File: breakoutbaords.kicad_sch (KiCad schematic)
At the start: 12 parts, among them J13 USB_A, J15 Conn_01x16, J16 Conn_01x16, J3 Conn_01x12, J4 Conn_01x12, U3 AMS1117-3.3

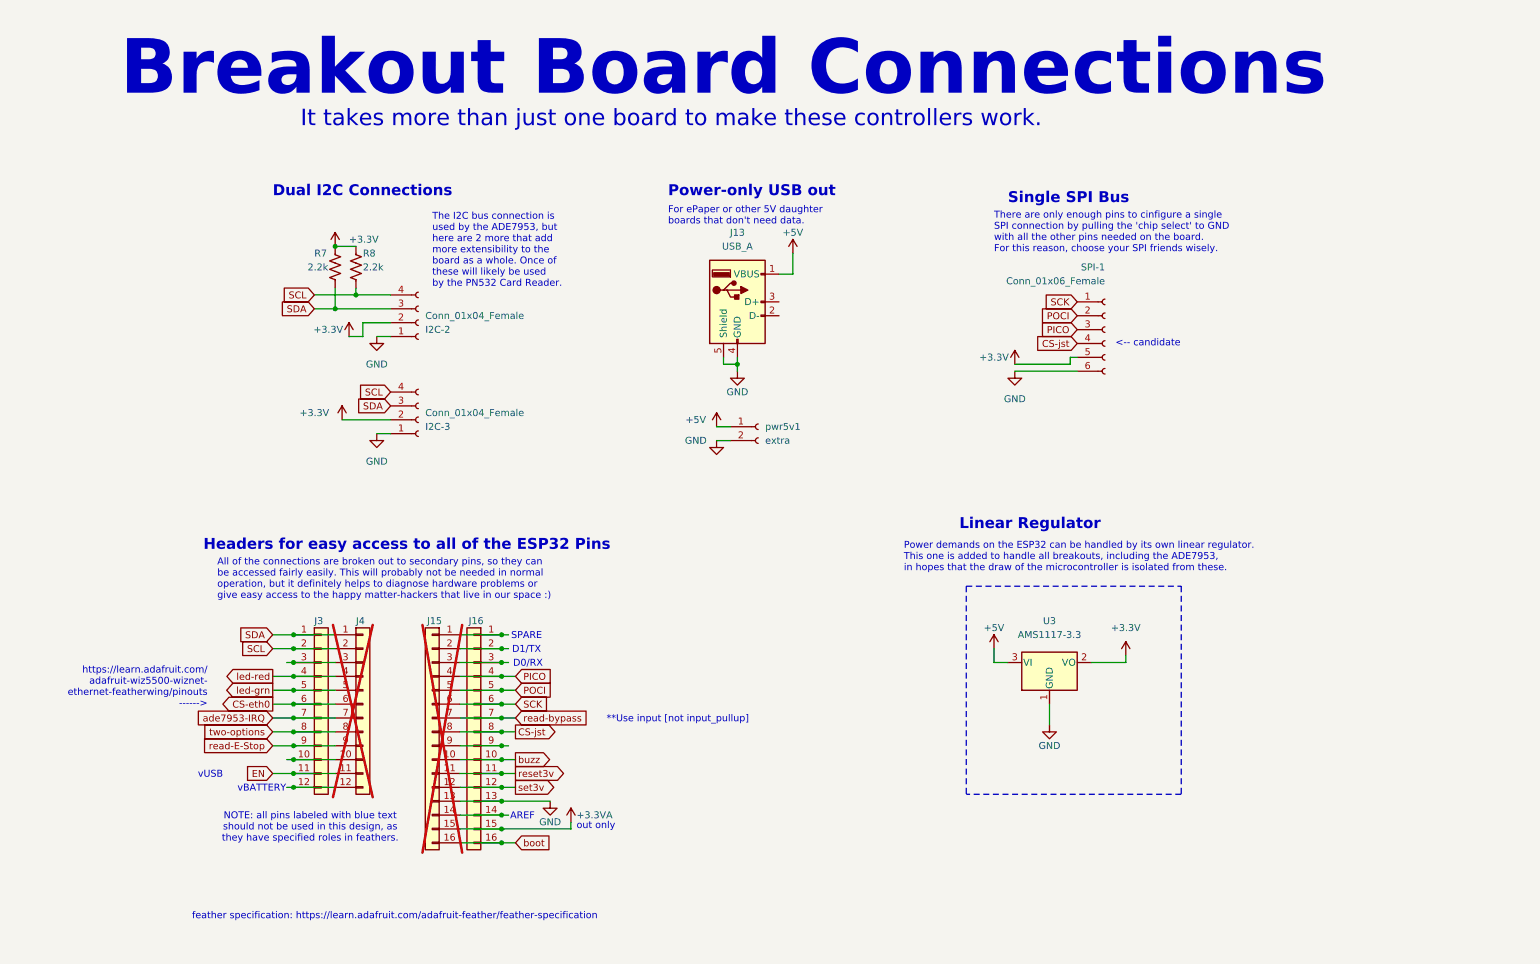
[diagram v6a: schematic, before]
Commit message: [fix] PICO/POCI flipped on Feather Boards
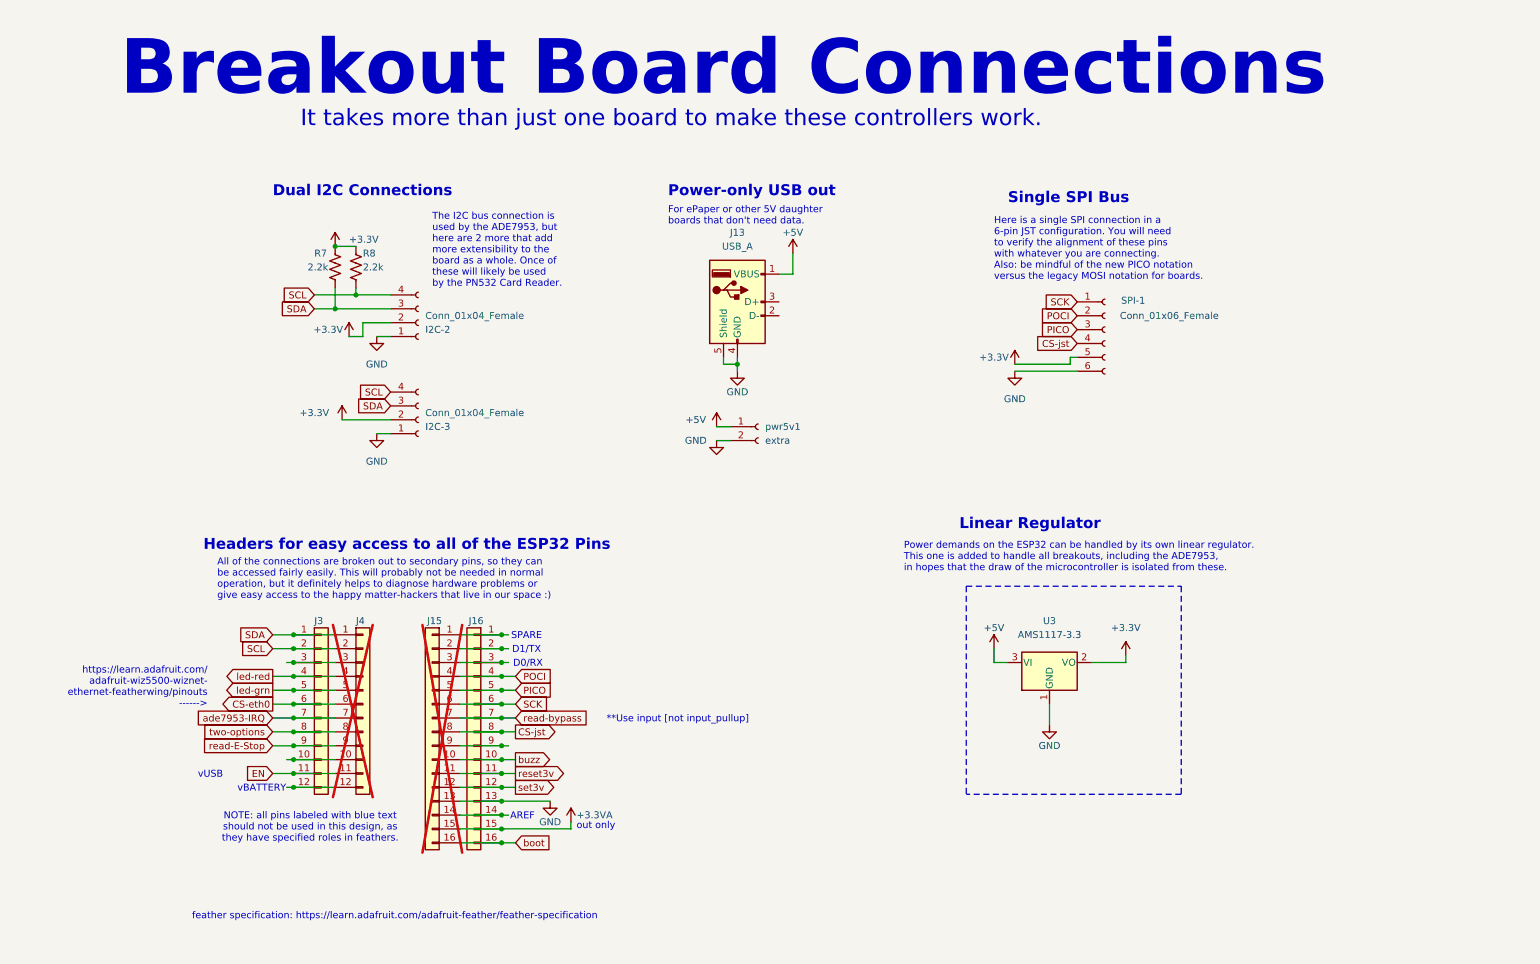
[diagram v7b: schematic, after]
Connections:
- net PICO: now also J15.5 (Pin_5), J16.5 (Pin_5); no longer J15.4 (Pin_4), J16.4 (Pin_4)
- net POCI: now also J15.4 (Pin_4), J16.4 (Pin_4); no longer J15.5 (Pin_5), J16.5 (Pin_5)
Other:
- note added: "Here is a single SPI connection in a 6-pin JST configuration. You will need to verify the alignment of these pins with whatever you are connecting. Also: be mindful of the new PICO notation versus the legacy MOSI notation for boards."
- note removed: "<-- candidate"
- note removed: "There are only enough pins to cinfigure a single SPI connection by pulling the 'chip select' to GND with all the other pins needed on the board. For this reason, choose your SPI friends wisely."
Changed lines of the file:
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@@
+	)
+	(junction
+		(at 60.96 158.75)
+		(diameter 0)
+		(color 0 0 0 0)
+	)
+	(junction
+		(at 60.96 140.97)
+		(diameter 0)
+		(color 0 0 0 0)
+	)
+	(junction
+		(at 60.96 161.29)
+		(diameter 0)
+		(color 0 0 0 0)
+	)
+	(junction
+		(at 68.58 78.74)
+		(diameter 0)
+		(color 0 0 0 0)
+	)
+	(junction
+		(at 72.39 76.2)
+		(diameter 0)
+		(color 0 0 0 0)
+	)
+	(junction
+		(at 99.06 171.45)
+		(diameter 0)
+		(color 0 0 0 0)
+	)
+	(junction
+		(at 99.06 161.29)
+		(diameter 0)
+		(color 0 0 0 0)
+	)
+	(junction
+		(at 99.06 156.21)
+		(diameter 0)
+		(color 0 0 0 0)
+	)
+	(junction
+		(at 99.06 173.99)
+		(diameter 0)
+		(color 0 0 0 0)
+	)
+	(junction
+		(at 60.96 148.59)
+		(diameter 0)
+		(color 0 0 0 0)
 	)
 	(junction
@@
 	)
 	(junction
-		(at 60.96 158.75)
-		(diameter 0)
-		(color 0 0 0 0)
-	)
-	(junction
-		(at 60.96 140.97)
-		(diameter 0)
-		(color 0 0 0 0)
-	)
-	(junction
-		(at 60.96 161.29)
-		(diameter 0)
-		(color 0 0 0 0)
-	)
-	(junction
-		(at 68.58 78.74)
-		(diameter 0)
-		(color 0 0 0 0)
-	)
-	(junction
-		(at 72.39 76.2)
-		(diameter 0)
-		(color 0 0 0 0)
-	)
-	(junction
-		(at 99.06 171.45)
-		(diameter 0)
-		(color 0 0 0 0)
-	)
-	(junction
-		(at 99.06 161.29)
-		(diameter 0)
-		(color 0 0 0 0)
-	)
-	(junction
-		(at 99.06 156.21)
-		(diameter 0)
-		(color 0 0 0 0)
-	)
-	(junction
-		(at 99.06 173.99)
-		(diameter 0)
-		(color 0 0 0 0)
-	)
-	(junction
-		(at 60.96 148.59)
-		(diameter 0)
-		(color 0 0 0 0)
-	)
-	(junction
 		(at 142.24 88.9)
 		(diameter 0)
@@
 	(wire
 		(pts
+			(xy 101.6 146.05) (xy 99.06 146.05)
+		)
+		(stroke
+			(width 0)
+			(type default)
+		)
+	)
+	(wire
+		(pts
 			(xy 57.15 158.75) (xy 60.96 158.75)
 		)
@@
 	(wire
 		(pts
-			(xy 99.06 148.59) (xy 101.6 148.59)
-		)
-		(stroke
-			(width 0)
-			(type default)
-		)
-	)
-	(wire
-		(pts
 			(xy 91.44 163.83) (xy 99.06 163.83)
 		)
@@
 	(wire
 		(pts
+			(xy 101.6 148.59) (xy 99.06 148.59)
+		)
+		(stroke
+			(width 0)
+			(type default)
+		)
+	)
+	(wire
+		(pts
 			(xy 189.23 143.51) (xy 191.77 143.51)
 		)
@@
 		(pts
 			(xy 99.06 176.53) (xy 101.6 176.53)
-		)
-		(stroke
-			(width 0)
-			(type default)
-		)
-	)
-	(wire
-		(pts
-			(xy 99.06 146.05) (xy 101.6 146.05)
 		)
 		(stroke
@@
 		)
 	)
-	(text "<-- candidate"
-		(exclude_from_sim no)
-		(at 217.424 85.09 0)
-		(effects
-			(font
-				(size 1.27 1.27)
-			)
-		)
-	)
-	(text "There are only enough pins to cinfigure a single \nSPI connection by pulling the 'chip select' to GND\nwith all the other pins needed on the board.\nFor this reason, choose your SPI friends wisely."
-		(exclude_from_sim no)
-		(at 189.23 68.58 0)
+	(text "Here is a single SPI connection in a\n6-pin JST configuration. You will need\nto verify the alignment of these pins\nwith whatever you are connecting.\nAlso: be mindful of the new PICO notation \nversus the legacy MOSI notation for boards."
+		(exclude_from_sim no)
+		(at 189.23 73.66 0)
 		(effects
 			(font
@@
 	(global_label "POCI"
 		(shape input)
-		(at 101.6 148.59 0)
+		(at 101.6 146.05 0)
 		(fields_autoplaced yes)
 		(effects
@@
 		)
 		(property "Intersheetrefs" "${INTERSHEET_REFS}"
-			(at 109.0605 148.59 0)
+			(at 109.0605 146.05 0)
 			(effects
 				(font
@@
 	(global_label "PICO"
 		(shape input)
-		(at 101.6 146.05 0)
+		(at 101.6 148.59 0)
 		(fields_autoplaced yes)
 		(effects
@@
 		)
 		(property "Intersheetrefs" "${INTERSHEET_REFS}"
-			(at 109.0605 146.05 0)
+			(at 109.0605 148.59 0)
 			(effects
 				(font
@@
 		(dnp no)
 		(property "Reference" "SPI-1"
-			(at 209.55 71.12 0)
+			(at 216.916 77.216 0)
 			(effects
 				(font
@@
 		)
 		(property "Value" "Conn_01x06_Female"
-			(at 209.55 73.66 0)
-			(effects
-				(font
+			(at 230.378 80.01 0)
+			(effects
+				(font

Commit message: added USBC for power. Changed Feather power-supply to be incompliance with Feather's recommendations
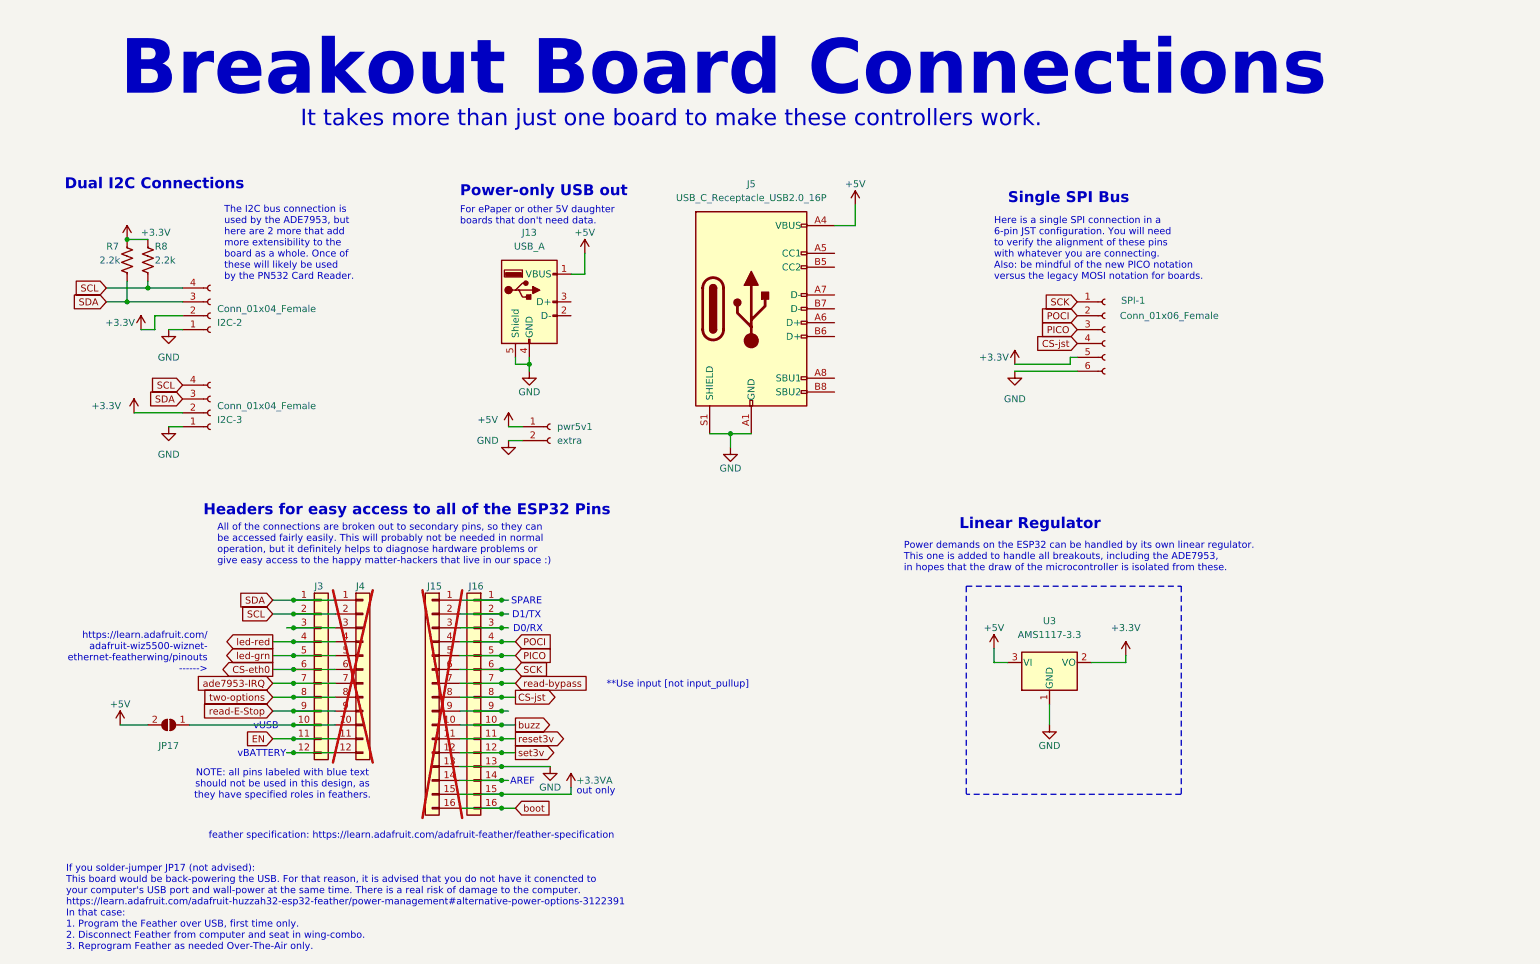
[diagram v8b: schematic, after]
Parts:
- added J5: USB_C_Receptacle_USB2.0_16P, usbc:USB-C-TH_GT-USB-7055, symbol Connector:USB_C_Receptacle_USB2.0_16P
- added JP17: no-filter-1, Jumper:SolderJumper-2_P1.3mm_Open_RoundedPad1.0x1.5mm, symbol Jumper:SolderJumper_2_Open
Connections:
- net +5V: now also J5.A4 (VBUS), J5.A9 (VBUS), J5.B4 (VBUS), J5.B9 (VBUS), JP17.2 (B)
- net GND: now also J5.A1 (GND), J5.A12 (GND), J5.B1 (GND), J5.B12 (GND), J5.S1 (SHIELD)
- net at J3.10 (Pin_10), J4.10 (Pin_10): now also JP17.1 (A)
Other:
- note added: "If you solder-jumper JP17 (not advised): This board would be back-powering the USB. For that reason, it is advised that you do not have it conencted to your computer's USB port and wall-power at the same time. There is a real risk of damage to the computer. https://learn.adafruit.com/adafruit-huzzah32-esp32-feather/power-management#alternative-power-options-3122391 In that case: 1. Program the Fe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"
- moved on the sheet: I2C-2, I2C-3, J13, J15, J16, J3, J4, R7, R8, pwr5v1
